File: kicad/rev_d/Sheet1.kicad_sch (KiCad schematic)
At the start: 163 parts, among them J1 JUMPER, J2 JUMPER, J3 JUMPER, J4 JUMPER, J7 JUMPER, Q1 14Mhz, X1 FDD34M, X2 IDE40M, X3 IDC26LPT, X7 DB15VGA, X8 PLB1-4I, X9 PLB1-2

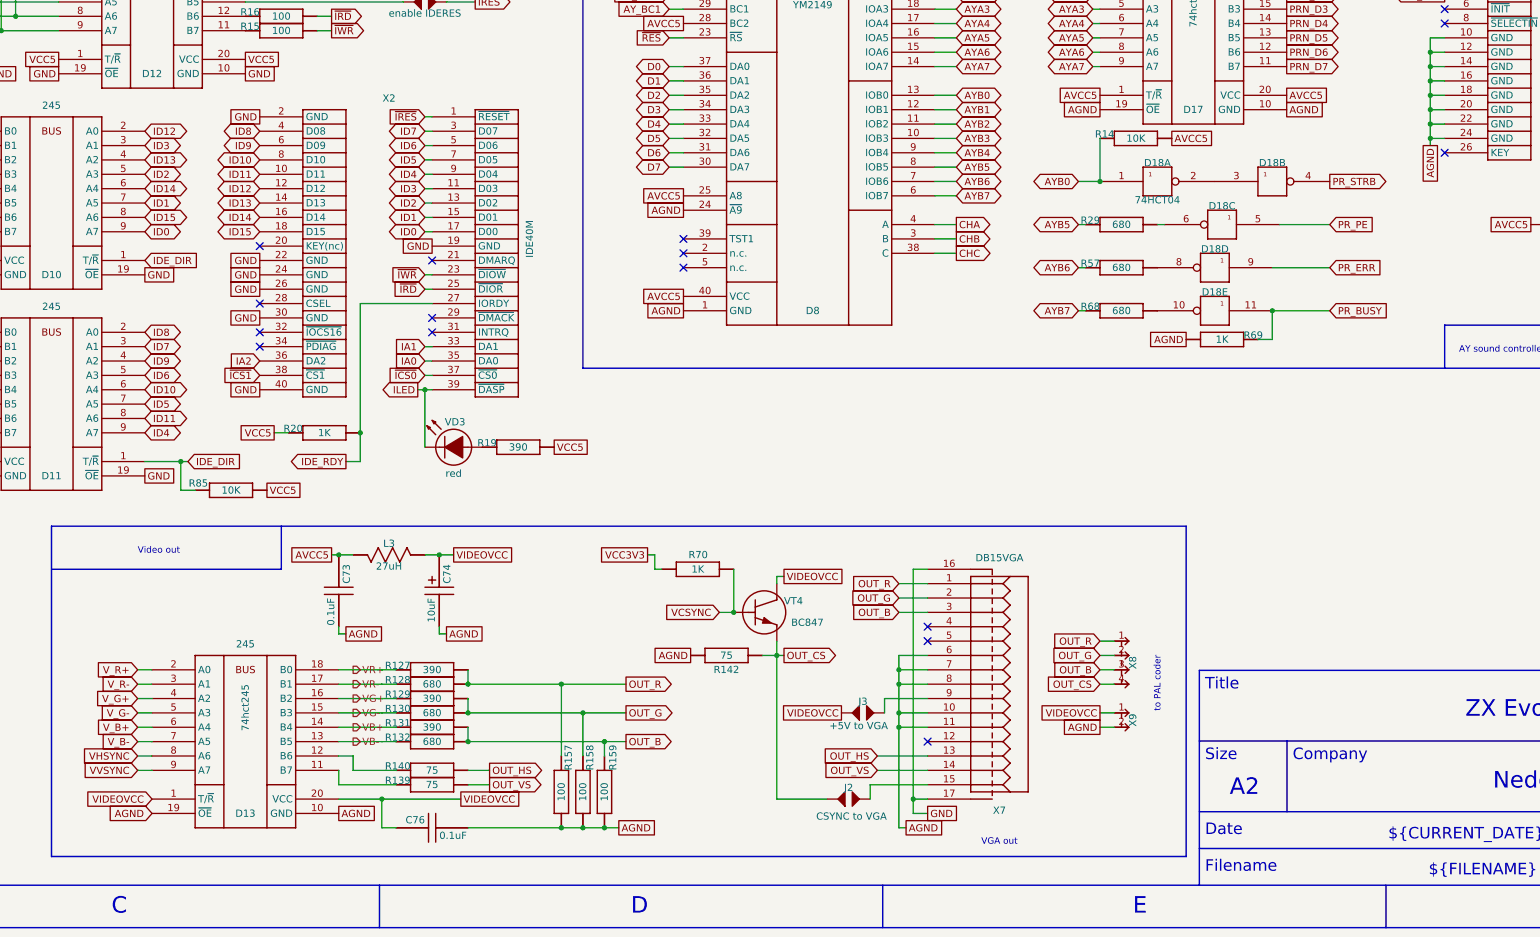
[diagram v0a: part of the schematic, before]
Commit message: pentevo: rev D: remove AGND, use GND instead
git-svn-id: svn://localhost/local-pentevo@1211 c6c76956-fad2-4150-a3a9-ea0a427205ba
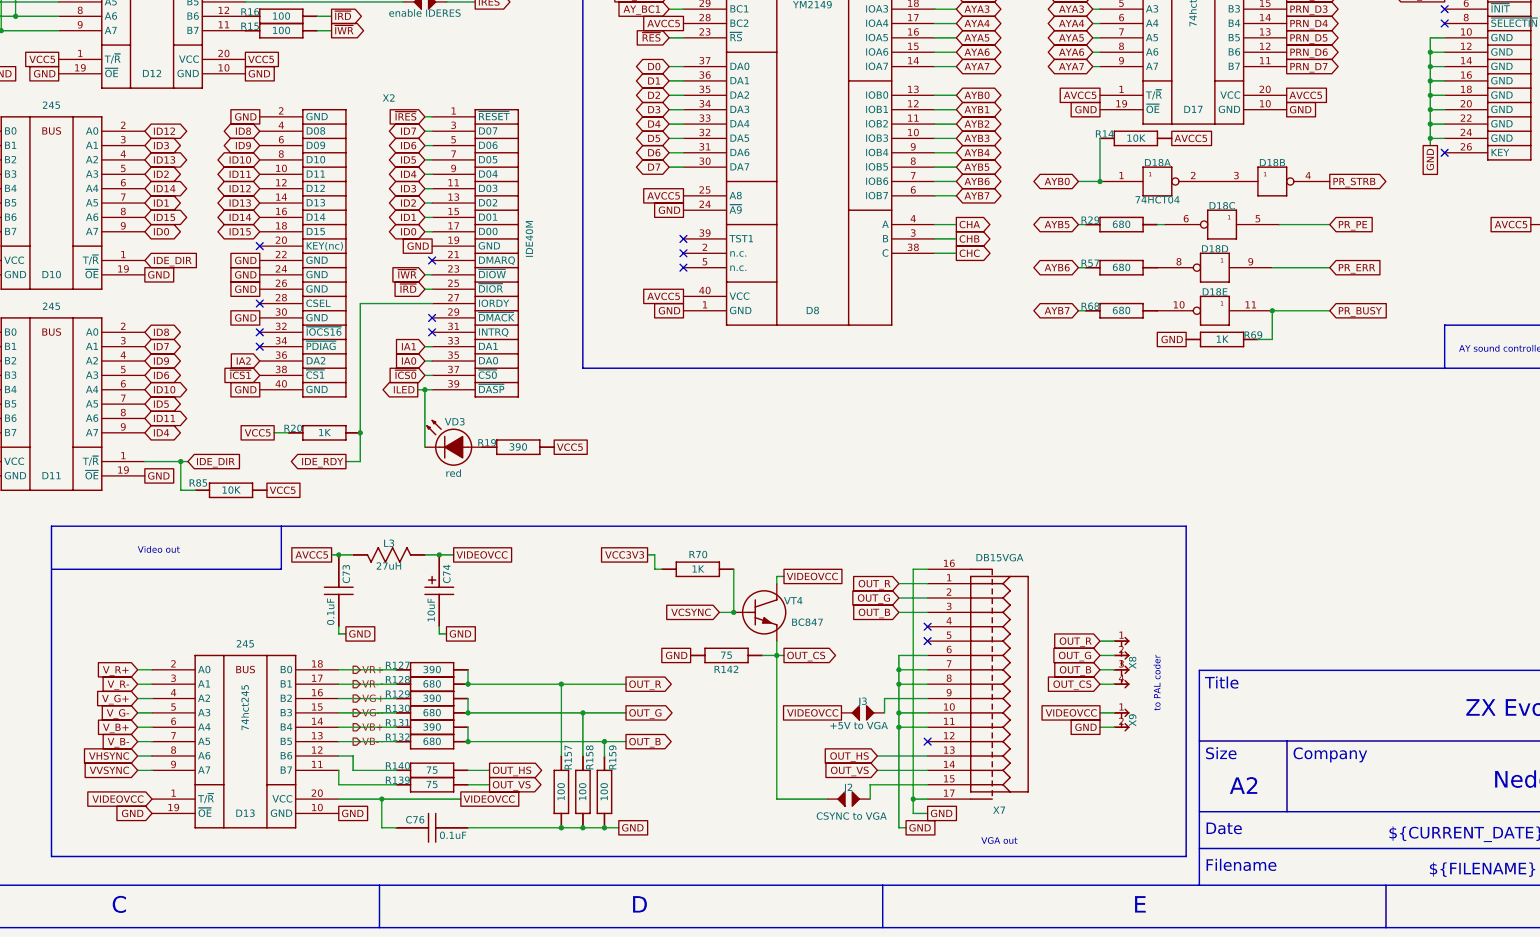
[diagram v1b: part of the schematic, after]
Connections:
- net AGND is gone; now on net GND: C73.2, C74.2, C76.2, D13.10 (GND), D13.19 (~{OE}), D17.10 (GND), D17.19 (~{OE}), D8.1 (GND), D8.24 (~{A9}), R142.1 (i/o), R157.1 (i/o), R158.1 (i/o), R159.1 (i/o), R69.1 (i/o), X3.10 (GND), X3.12 (GND), X3.14 (GND), X3.16 (GND), X3.18 (GND), X3.20 (GND), X3.22 (GND), X3.24 (GND), X7.10, X7.11, X7.6, X7.7, X7.8, X9.2
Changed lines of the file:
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@@
 		)
 	)
-	(global_label "AGND"
+	(global_label "GND"
 		(shape passive)
 		(at 439.42 274.32 0)
@@
 		)
 		(property "Intersheetrefs" "${INTERSHEET_REFS}"
-			(at 446.253 274.32 0)
+			(at 445.1644 274.32 0)
 			(effects
 				(font
@@
 		)
 	)
-	(global_label "AGND"
+	(global_label "GND"
 		(shape passive)
 		(at 321.31 401.32 0)
@@
 		)
 		(property "Intersheetrefs" "${INTERSHEET_REFS}"
-			(at 328.143 401.32 0)
+			(at 327.0544 401.32 0)
 			(effects
 				(font
@@
 		)
 	)
-	(global_label "AGND"
+	(global_label "GND"
 		(shape passive)
 		(at 334.01 370.84 180)
@@
 		)
 		(property "Intersheetrefs" "${INTERSHEET_REFS}"
-			(at 327.177 370.84 0)
+			(at 328.2656 370.84 0)
 			(effects
 				(font
@@
 		)
 	)
-	(global_label "AGND"
+	(global_label "GND"
 		(shape passive)
 		(at 406.4 274.32 180)
@@
 		)
 		(property "Intersheetrefs" "${INTERSHEET_REFS}"
-			(at 399.567 274.32 0)
+			(at 400.6556 274.32 0)
 			(effects
 				(font
@@
 		)
 	)
-	(global_label "AGND"
+	(global_label "GND"
 		(shape passive)
 		(at 421.64 314.96 180)
@@
 		)
 		(property "Intersheetrefs" "${INTERSHEET_REFS}"
-			(at 414.807 314.96 0)
+			(at 415.8956 314.96 0)
 			(effects
 				(font
@@
 		)
 	)
-	(global_label "AGND"
+	(global_label "GND"
 		(shape passive)
 		(at 290.83 367.03 0)
@@
 		)
 		(property "Intersheetrefs" "${INTERSHEET_REFS}"
-			(at 297.663 367.03 0)
+			(at 296.5744 367.03 0)
 			(effects
 				(font
@@
 		)
 	)
-	(global_label "AGND"
+	(global_label "GND"
 		(shape passive)
 		(at 271.78 398.78 0)
@@
 		)
 		(property "Intersheetrefs" "${INTERSHEET_REFS}"
-			(at 278.613 398.78 0)
+			(at 277.5244 398.78 0)
 			(effects
 				(font
@@
 		)
 	)
-	(global_label "AGND"
+	(global_label "GND"
 		(shape passive)
 		(at 406.4 383.54 180)
@@
 		)
 		(property "Intersheetrefs" "${INTERSHEET_REFS}"
-			(at 399.567 383.54 0)
+			(at 400.6556 383.54 0)
 			(effects
 				(font
@@
 		)
 	)
-	(global_label "AGND"
+	(global_label "GND"
 		(shape passive)
 		(at 372.11 401.32 0)
@@
 		)
 		(property "Intersheetrefs" "${INTERSHEET_REFS}"
-			(at 378.943 401.32 0)
+			(at 377.8544 401.32 0)
 			(effects
 				(font
@@
 		)
 	)
-	(global_label "AGND"
+	(global_label "GND"
 		(shape passive)
 		(at 332.74 292.1 180)
@@
 		)
 		(property "Intersheetrefs" "${INTERSHEET_REFS}"
-			(at 325.907 292.1 0)
+			(at 326.9956 292.1 0)
 			(effects
 				(font
@@
 		)
 	)
-	(global_label "AGND"
+	(global_label "GND"
 		(shape passive)
 		(at 332.74 309.88 180)
@@
 		)
 		(property "Intersheetrefs" "${INTERSHEET_REFS}"
-			(at 325.907 309.88 0)
+			(at 326.9956 309.88 0)
 			(effects
 				(font
@@
 		)
 	)
-	(global_label "AGND"
+	(global_label "GND"
 		(shape input)
 		(at 238.76 398.78 180)
@@
 		)
 		(property "Intersheetrefs" "${INTERSHEET_REFS}"
-			(at 230.8157 398.78 0)
+			(at 231.9043 398.78 0)
 			(effects
 				(font
@@
 		)
 	)
-	(global_label "AGND"
+	(global_label "GND"
 		(shape passive)
 		(at 273.05 367.03 0)
@@
 		)
 		(property "Intersheetrefs" "${INTERSHEET_REFS}"
-			(at 279.883 367.03 0)
+			(at 278.7944 367.03 0)
 			(effects
 				(font
@@
 		)
 	)
-	(global_label "AGND"
+	(global_label "GND"
 		(shape passive)
 		(at 464.82 280.67 270)
@@
 		)
 		(property "Intersheetrefs" "${INTERSHEET_REFS}"
-			(at 464.82 287.503 90)
+			(at 464.82 286.4144 90)
 			(effects
 				(font

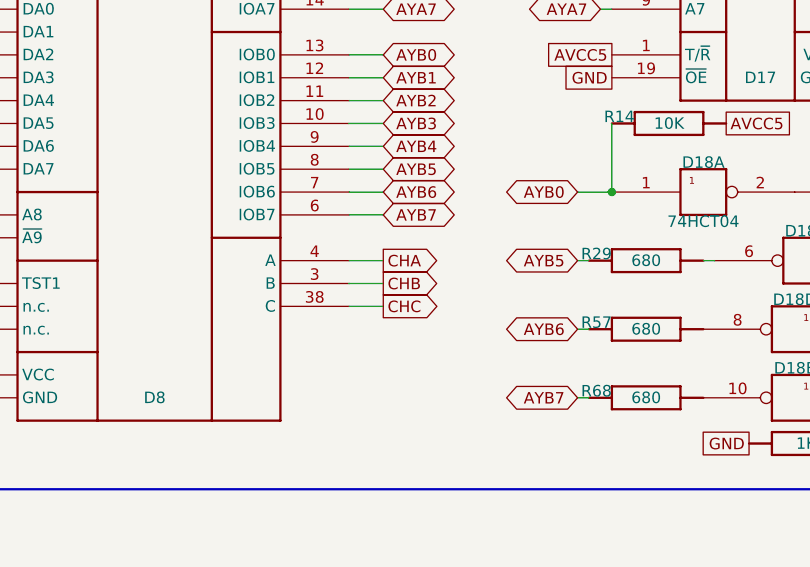
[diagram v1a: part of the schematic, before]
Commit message: pentevo: rev D: start redoing audio part (WIP)
git-svn-id: svn://localhost/local-pentevo@1219 c6c76956-fad2-4150-a3a9-ea0a427205ba
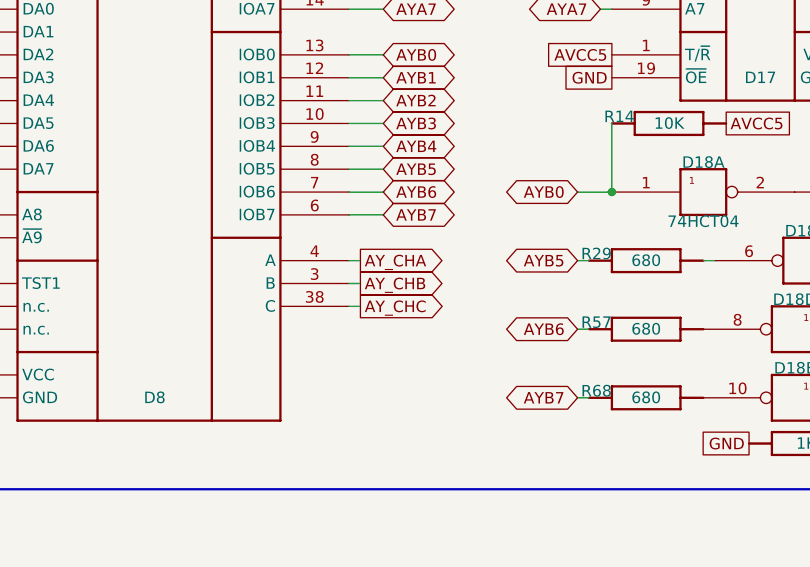
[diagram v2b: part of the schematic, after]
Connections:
- net CHA renamed AY_CHA
- net CHB renamed AY_CHB
- net CHC renamed AY_CHC
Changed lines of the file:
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@@
 	(wire
 		(pts
-			(xy 381 299.72) (xy 377.19 299.72)
+			(xy 378.46 299.72) (xy 377.19 299.72)
 		)
 		(stroke
@@
 	(wire
 		(pts
-			(xy 381 294.64) (xy 377.19 294.64)
-		)
-		(stroke
-			(width 0)
-			(type default)
-		)
-	)
-	(wire
-		(pts
 			(xy 119.38 304.8) (xy 121.92 304.8)
 		)
@@
 	(wire
 		(pts
+			(xy 378.46 294.64) (xy 377.19 294.64)
+		)
+		(stroke
+			(width 0)
+			(type default)
+		)
+	)
+	(wire
+		(pts
 			(xy 457.2 92.71) (xy 462.28 92.71)
 		)
@@
 	(wire
 		(pts
-			(xy 381 297.18) (xy 377.19 297.18)
+			(xy 378.46 297.18) (xy 377.19 297.18)
 		)
 		(stroke
@@
 		)
 	)
-	(global_label "CHC"
+	(global_label "AY_CHC"
 		(shape output)
-		(at 381 299.72 0)
+		(at 378.46 299.72 0)
 		(fields_autoplaced yes)
 		(effects
@@
 		)
 		(property "Intersheetrefs" "${INTERSHEET_REFS}"
-			(at 387.8557 299.72 0)
+			(at 385.3157 299.72 0)
 			(effects
 				(font
@@
 		)
 	)
-	(global_label "CHA"
+	(global_label "AY_CHA"
 		(shape output)
-		(at 381 294.64 0)
+		(at 378.46 294.64 0)
 		(fields_autoplaced yes)
 		(effects
@@
 		)
 		(property "Intersheetrefs" "${INTERSHEET_REFS}"
-			(at 387.6743 294.64 0)
+			(at 385.1343 294.64 0)
 			(effects
 				(font
@@
 		)
 	)
-	(global_label "CHB"
+	(global_label "AY_CHB"
 		(shape output)
-		(at 381 297.18 0)
+		(at 378.46 297.18 0)
 		(fields_autoplaced yes)
 		(effects
@@
 		)
 		(property "Intersheetrefs" "${INTERSHEET_REFS}"
-			(at 387.8557 297.18 0)
+			(at 385.3157 297.18 0)
 			(effects
 				(font

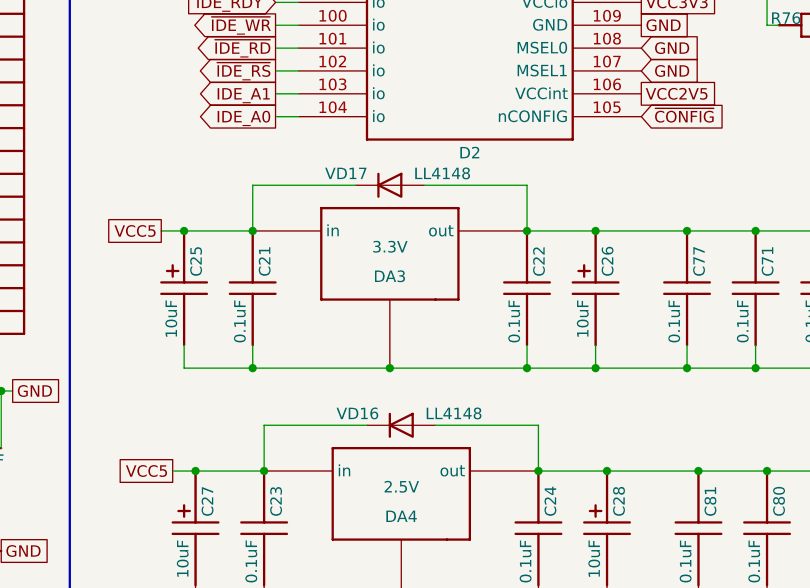
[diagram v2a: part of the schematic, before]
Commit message: pentevo: rev D: redoing audio (WIP), add reverse diodes to linear regulators
git-svn-id: svn://localhost/local-pentevo@1221 c6c76956-fad2-4150-a3a9-ea0a427205ba
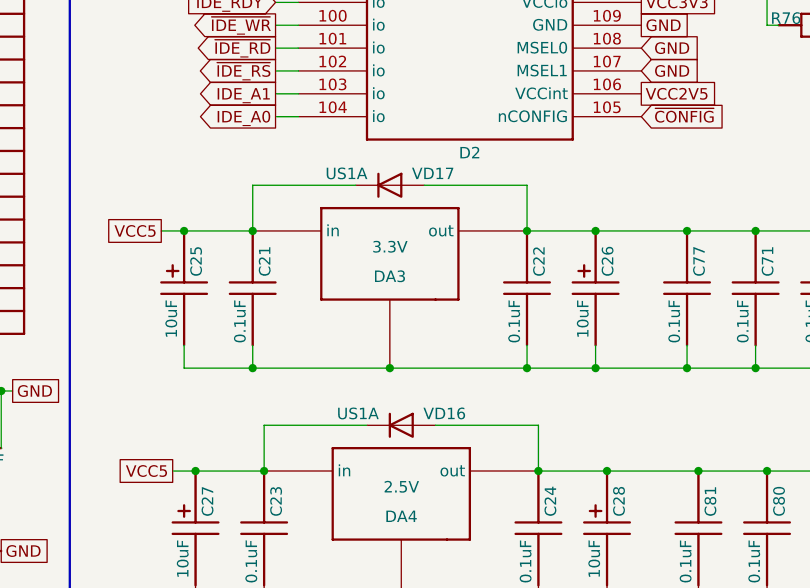
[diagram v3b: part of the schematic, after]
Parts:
- removed VD16, VD17: LL4148, Diode_SMD:D_MiniMELF_Handsoldering, symbol Diode:LL4148
- added VD16, VD17: US1A, Diode_SMD:D_SMA, symbol Diode:US1A
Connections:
- net VCC2V5: now also VD16.2 (A)
- net VCC3V3: now also VD17.2 (A)
- net VCC5: now also VD16.1 (K), VD17.1 (K)
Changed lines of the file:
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@@
 	)
 	(symbol
-		(lib_id "Diode:LL4148")
-		(at 133.35 387.35 0)
-		(unit 1)
-		(exclude_from_sim no)
-		(in_bom yes)
-		(on_board yes)
-		(dnp no)
-		(property "Reference" "VD16"
-			(at 128.524 386.08 0)
-			(effects
-				(font
-					(size 1.27 1.27)
-				)
-			)
-		)
-		(property "Value" "LL4148"
-			(at 139.192 386.08 0)
-			(effects
-				(font
-					(size 1.27 1.27)
-				)
-			)
-		)
-		(property "Footprint" "Diode_SMD:D_MiniMELF_Handsoldering"
-			(at 133.35 391.795 0)
-			(effects
-				(font
-					(size 1.27 1.27)
-				)
-				(hide yes)
-			)
-		)
-		(property "Datasheet" "http://www.vishay.com/docs/85557/ll4148.pdf"
-			(at 133.35 387.35 0)
-			(effects
-				(font
-					(size 1.27 1.27)
-				)
-				(hide yes)
-			)
-		)
-		(property "Description" "100V 0.15A standard switching diode, MiniMELF"
-			(at 133.35 387.35 0)
-			(effects
-				(font
-					(size 1.27 1.27)
-				)
-				(hide yes)
-			)
-		)
-		(property "Sim.Device" "D"
-			(at 133.35 387.35 0)
-			(effects
-				(font
-					(size 1.27 1.27)
-				)
-				(hide yes)
-			)
-		)
-		(property "Sim.Pins" "1=K 2=A"
-			(at 133.35 387.35 0)
-			(effects
-				(font
-					(size 1.27 1.27)
-				)
-				(hide yes)
-			)
-		)
-		(pin "2"
-		)
-		(pin "1"
-		)
-		(instances
-			(project ""
-				(path "/ab605654-a730-497b-9e09-9b351f74b935/df95af23-acf0-4751-87c3-fbc71e0508c6"
-					(reference "VD16")
-					(unit 1)
-				)
-			)
-		)
-	)
-	(symbol
 		(lib_id "eva-altium-import:Sheet1_0_CAPCHIP")
 		(at 280.67 245.11 0)
@@
 	)
 	(symbol
+		(lib_id "Diode:US1A")
+		(at 133.35 387.35 0)
+		(unit 1)
+		(exclude_from_sim no)
+		(in_bom yes)
+		(on_board yes)
+		(dnp no)
+		(property "Reference" "VD16"
+			(at 138.176 386.08 0)
+			(effects
+				(font
+					(size 1.27 1.27)
+				)
+			)
+		)
+		(property "Value" "US1A"
+			(at 128.524 386.08 0)
+			(effects
+				(font
+					(size 1.27 1.27)
+				)
+			)
+		)
+		(property "Footprint" "Diode_SMD:D_SMA"
+			(at 133.35 391.795 0)
+			(effects
+				(font
+					(size 1.27 1.27)
+				)
+				(hide yes)
+			)
+		)
+		(property "Datasheet" "https://www.diodes.com/assets/Datasheets/ds16008.pdf"
+			(at 133.35 387.35 0)
+			(effects
+				(font
+					(size 1.27 1.27)
+				)
+				(hide yes)
+			)
+		)
+		(property "Description" "50V, 1A, General Purpose Rectifier Diode, SMA(DO-214AC)"
+			(at 133.35 387.35 0)
+			(effects
+				(font
+					(size 1.27 1.27)
+				)
+				(hide yes)
+			)
+		)
+		(property "Sim.Device" "D"
+			(at 133.35 387.35 0)
+			(effects
+				(font
+					(size 1.27 1.27)
+				)
+				(hide yes)
+			)
+		)
+		(property "Sim.Pins" "1=K 2=A"
+			(at 133.35 387.35 0)
+			(effects
+				(font
+					(size 1.27 1.27)
+				)
+				(hide yes)
+			)
+		)
+		(pin "1"
+		)
+		(pin "2"
+		)
+		(instances
+			(project "eva"
+				(path "/ab605654-a730-497b-9e09-9b351f74b935/df95af23-acf0-4751-87c3-fbc71e0508c6"
+					(reference "VD16")
+					(unit 1)
+				)
+			)
+		)
+	)
+	(symbol
 		(lib_id "eva-altium-import:Sheet1_0_CDR64B")
 		(at 274.32 353.06 0)
@@
 	)
 	(symbol
-		(lib_id "Diode:LL4148")
-		(at 132.08 360.68 0)
-		(unit 1)
-		(exclude_from_sim no)
-		(in_bom yes)
-		(on_board yes)
-		(dnp no)
-		(property "Reference" "VD17"
-			(at 127.254 359.41 0)
-			(effects
-				(font
-					(size 1.27 1.27)
-				)
-			)
-		)
-		(property "Value" "LL4148"
-			(at 137.922 359.41 0)
-			(effects
-				(font
-					(size 1.27 1.27)
-				)
-			)
-		)
-		(property "Footprint" "Diode_SMD:D_MiniMELF_Handsoldering"
-			(at 132.08 365.125 0)
-			(effects
-				(font
-					(size 1.27 1.27)
-				)
-				(hide yes)
-			)
-		)
-		(property "Datasheet" "http://www.vishay.com/docs/85557/ll4148.pdf"
-			(at 132.08 360.68 0)
-			(effects
-				(font
-					(size 1.27 1.27)
-				)
-				(hide yes)
-			)
-		)
-		(property "Description" "100V 0.15A standard switching diode, MiniMELF"
-			(at 132.08 360.68 0)
-			(effects
-				(font
-					(size 1.27 1.27)
-				)
-				(hide yes)
-			)
-		)
-		(property "Sim.Device" "D"
-			(at 132.08 360.68 0)
-			(effects
-				(font
-					(size 1.27 1.27)
-				)
-				(hide yes)
-			)
-		)
-		(property "Sim.Pins" "1=K 2=A"
-			(at 132.08 360.68 0)
-			(effects
-				(font
-					(size 1.27 1.27)
-				)
-				(hide yes)
-			)
-		)
-		(pin "2"
-		)
-		(pin "1"
-		)
-		(instances
-			(project "eva"
-				(path "/ab605654-a730-497b-9e09-9b351f74b935/df95af23-acf0-4751-87c3-fbc71e0508c6"
-					(reference "VD17")
-					(unit 1)
-				)
-			)
-		)
-	)
-	(symbol
 		(lib_id "eva-altium-import:Sheet1_0_Z84C0020FEC")
 		(at 30.48 54.61 0)
@@
 					(unit 1)
 				)
+			)
+		)
+	)
+	(symbol
+		(lib_id "Diode:US1A")
+		(at 132.08 360.68 0)
+		(unit 1)
+		(exclude_from_sim no)
+		(in_bom yes)
+		(on_board yes)
+		(dnp no)
+		(property "Reference" "VD17"
+			(at 136.906 359.41 0)
+			(effects
+				(font
+					(size 1.27 1.27)
+				)
+			)
+		)
+		(property "Value" "US1A"
+			(at 127.254 359.41 0)
+			(effects
+				(font
+					(size 1.27 1.27)
+				)
+			)
+		)
+		(property "Footprint" "Diode_SMD:D_SMA"
+			(at 132.08 365.125 0)
+			(effects
+				(font
+					(size 1.27 1.27)
+				)
+				(hide yes)
+			)
+		)
+		(property "Datasheet" "https://www.diodes.com/assets/Datasheets/ds16008.pdf"
+			(at 132.08 360.68 0)
+			(effects
+				(font
+					(size 1.27 1.27)
+				)
+				(hide yes)
+			)
+		)
+		(property "Description" "50V, 1A, General Purpose Rectifier Diode, SMA(DO-214AC)"
+			(at 132.08 360.68 0)
+			(effects
+				(font
+					(size 1.27 1.27)
+				)
+				(hide yes)
+			)
+		)
+		(property "Sim.Device" "D"
+			(at 132.08 360.68 0)
+			(effects
+				(font
+					(size 1.27 1.27)
+				)
+				(hide yes)
+			)
+		)
+		(property "Sim.Pins" "1=K 2=A"
+			(at 132.08 360.68 0)
+			(effects
+				(font
+					(size 1.27 1.27)
+				)
+				(hide yes)
+			)
+		)
+		(pin "1"
+		)
+		(pin "2"
+		)
+		(instances
+			(project "eva"
+				(path "/ab605654-a730-497b-9e09-9b351f74b935/df95af23-acf0-4751-87c3-fbc71e0508c6"
+					(reference "VD17")
+					(unit 1)
+				)
